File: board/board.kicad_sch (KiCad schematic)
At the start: 14 parts, among them J1 Conn_01x02_Socket, J2 Barrel_Jack_Switch, Q1 NPN, U1 LM350_TO3, U2 NE555P, U3 LM350_TO3

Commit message: add link on schematic
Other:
- note added: "https://www.electronicshub.org/555-timer-pwm/"
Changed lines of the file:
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@@
+    (effects (font (size 1.27 1.27)) (justify left bottom))
+  )
+  (text "https://www.electronicshub.org/555-timer-pwm/" (at 76.962 138.684 0)
     (effects (font (size 1.27 1.27)) (justify left bottom))
   )

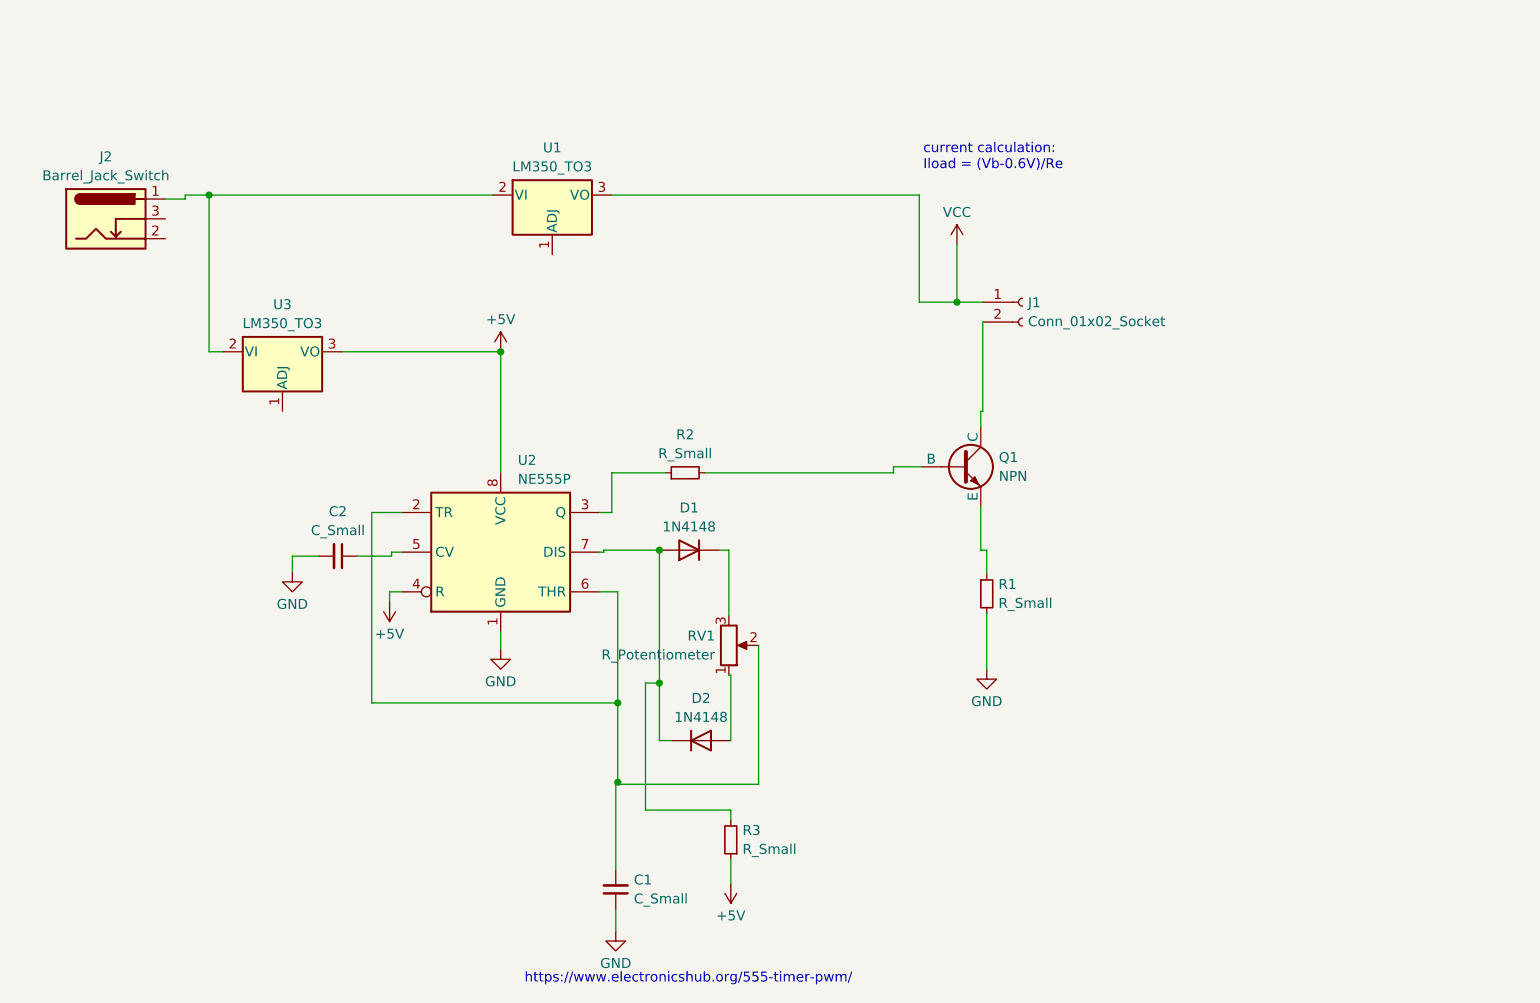
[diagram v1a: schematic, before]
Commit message: add first schematci version of LED driver
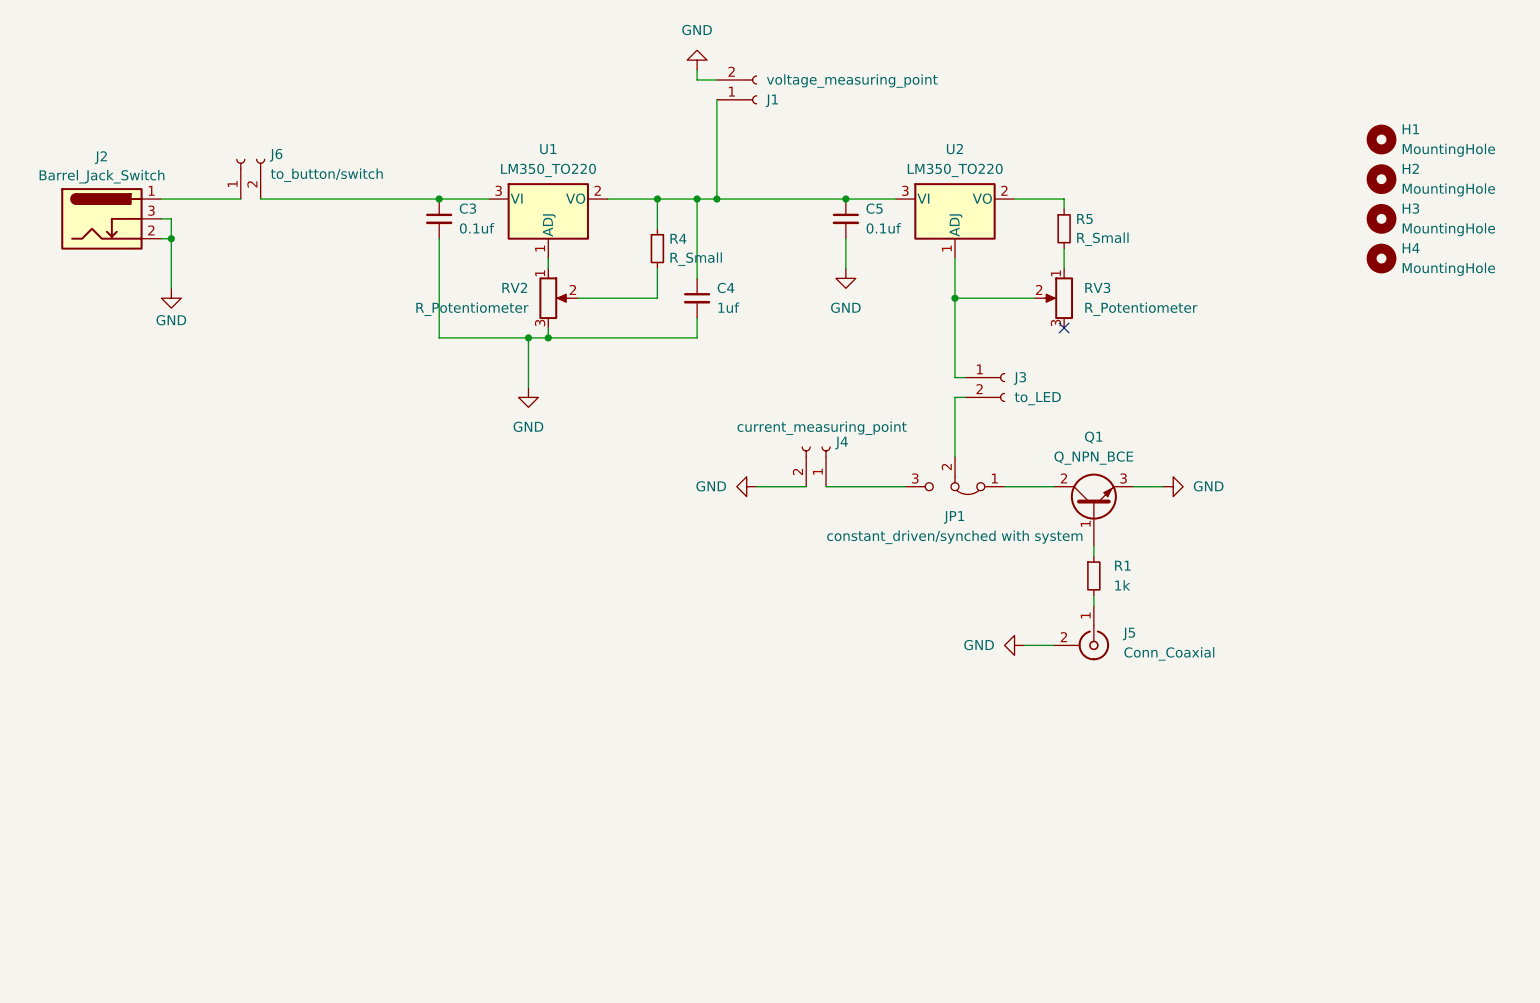
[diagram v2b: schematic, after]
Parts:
- removed C1, C2: C_Small, symbol Device:C_Small
- removed D1, D2: 1N4148, Diode_THT:D_DO-35_SOD27_P7.62mm_Horizontal, symbol Diode:1N4148
- removed Q1: NPN, symbol Simulation_SPICE:NPN
- removed R2, R3: R_Small, symbol Device:R_Small
- removed RV1: R_Potentiometer, symbol Device:R_Potentiometer
- removed U1, U3: LM350_TO3, Package_TO_SOT_THT:TO-3, symbol Regulator_Linear:LM350_TO3
- removed U2: NE555P, Package_DIP:DIP-8_W7.62mm, symbol Timer:NE555P
- added C3, C5: 0.1uf, Capacitor_THT:C_Disc_D9.0mm_W2.5mm_P5.00mm, symbol Device:C_Small
- added C4: 1uf, Capacitor_THT:CP_Radial_D10.0mm_P5.00mm, symbol Device:C_Small
- added H1, H2, H3, H4: MountingHole, MountingHole:MountingHole_3.2mm_M3, symbol Mechanical:MountingHole
- added J3: to_LED, Connector_JST:JST_XH_B2B-XH-A_1x02_P2.50mm_Vertical, symbol Connector:Conn_01x02_Socket
- added J4: current_measuring_point, Connector_JST:JST_XH_B2B-XH-A_1x02_P2.50mm_Vertical, symbol Connector:Conn_01x02_Socket
- added J5: Conn_Coaxial, Connector_JST:JST_XH_B2B-XH-A_1x02_P2.50mm_Vertical, symbol Connector:Conn_Coaxial
- added J6: to_button/switch, Connector_JST:JST_XH_B2B-XH-A_1x02_P2.50mm_Vertical, symbol Connector:Conn_01x02_Socket
- added JP1: constant_driven/synched with system, Connector_PinHeader_2.54mm:PinHeader_1x03_P2.54mm_Vertical, symbol Jumper:Jumper_3_Bridged12
- added Q1: Q_NPN_BCE, Package_TO_SOT_THT:TO-220-3_Vertical, symbol Device:Q_NPN_BCE
- added R4, R5: R_Small, Resistor_THT:R_Axial_DIN0411_L9.9mm_D3.6mm_P15.24mm_Horizontal, symbol Device:R_Small
- added RV2, RV3: R_Potentiometer, Connector_PinHeader_2.54mm:PinHeader_1x03_P2.54mm_Vertical, symbol Device:R_Potentiometer
- added U1, U2: LM350_TO220, Package_TO_SOT_THT:TO-220-3_Vertical, symbol Regulator_Linear:LM350_TO220
- J1: value Conn_01x02_Socket -> voltage_measuring_point; footprint (none) -> Connector_JST:JST_XH_B2B-XH-A_1x02_P2.50mm_Vertical
- J2: footprint (none) -> Connector_BarrelJack:BarrelJack_Horizontal
- R1: value R_Small -> 1k; footprint (none) -> Resistor_THT:R_Axial_DIN0411_L9.9mm_D3.6mm_P15.24mm_Horizontal
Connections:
- net GND: now also J1.2 (Pin_2), J2.2, J2.3, C3.2, C4.2, C5.2, J4.2 (Pin_2), J5.2 (Ext), Q1.3 (E), RV2.3; no longer R1.2
- net at R1.1: now also Q1.1 (B)
- net at J2.1: now also J6.1 (Pin_1)
- net VCC: no longer names the net of J1.1 (Pin_1)
- net VCC: now also C4.1, C5.1, R4.1, U1.2 (VO), U2.3 (VI)
- new net: J5.1 (In), R1.2
- new net: J3.1 (Pin_1), RV3.2, U2.1 (ADJ)
- new net: J3.2 (Pin_2), JP1.2 (C)
- new net: R5.1, U2.2 (VO)
- new net: R5.2, RV3.1
- new net: JP1.1 (A), Q1.2 (C)
- new net: J4.1 (Pin_1), JP1.3 (B)
- new net: RV2.1, U1.1 (ADJ)
- new net: C3.1, J6.2 (Pin_2), U1.3 (VI)
- new net: R4.2, RV2.2
- no-connect marks 0 -> 1
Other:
- note removed: "current calculation: Iload = (Vb-0.6V)/Re"
- note removed: "https://www.electronicshub.org/555-timer-pwm/"
- moved on the sheet: J2

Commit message: make first prototype and production files
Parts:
- removed J2: Barrel_Jack_Switch, Connector_BarrelJack:BarrelJack_Horizontal, symbol Connector:Barrel_Jack_Switch
- removed J6: to_button/switch, Connector_JST:JST_XH_B2B-XH-A_1x02_P2.50mm_Vertical, symbol Connector:Conn_01x02_Socket
- added D1: LED, LED_THT:LED_D5.0mm_Clear, symbol Device:LED
- added J2: Conn_01x03_Socket, Connector_JST:JST_XH_B3B-XH-A_1x03_P2.50mm_Vertical, symbol Connector:Conn_01x03_Socket
- added J7: Vin, Connector_JST:JST_XH_B2B-XH-A_1x02_P2.50mm_Vertical, symbol Connector:Conn_01x02_Socket
- added J8: Vin_relay, Connector_JST:JST_XH_B2B-XH-A_1x02_P2.50mm_Vertical, symbol Connector:Conn_01x02_Socket
- added R2: 1k, Resistor_THT:R_Axial_DIN0411_L9.9mm_D3.6mm_P15.24mm_Horizontal, symbol Device:R_Small
- added R3: 1M, Resistor_THT:R_Axial_DIN0411_L9.9mm_D3.6mm_P15.24mm_Horizontal, symbol Device:R_Small
- C4: symbol Device:C_Small -> Device:C_Polarized_Small
- R4: value R_Small -> 240
- R5: value R_Small -> 0.4ohm 2W
- RV2: value R_Potentiometer -> 5k
- RV3: value R_Potentiometer -> 10 ohm 2w
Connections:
- net GND: now also RV2.2, J2.3 (Pin_3), J7.2 (Pin_2), J8.2 (Pin_2), R2.1, R3.2; no longer RV2.3
- net at J3.1 (Pin_1), RV3.2, U2.1 (ADJ): now also R3.1
- net at RV2.1, U1.1 (ADJ): now also R4.2
- net at C3.1, U1.3 (VI): now also D1.2 (A), J2.2 (Pin_2)
- new net: D1.1 (K), R2.2
- new net +12V: J2.1 (Pin_1), J7.1 (Pin_1), J8.1 (Pin_1)
- no-connect marks 1 -> 2
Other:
- moved on the sheet: RV2

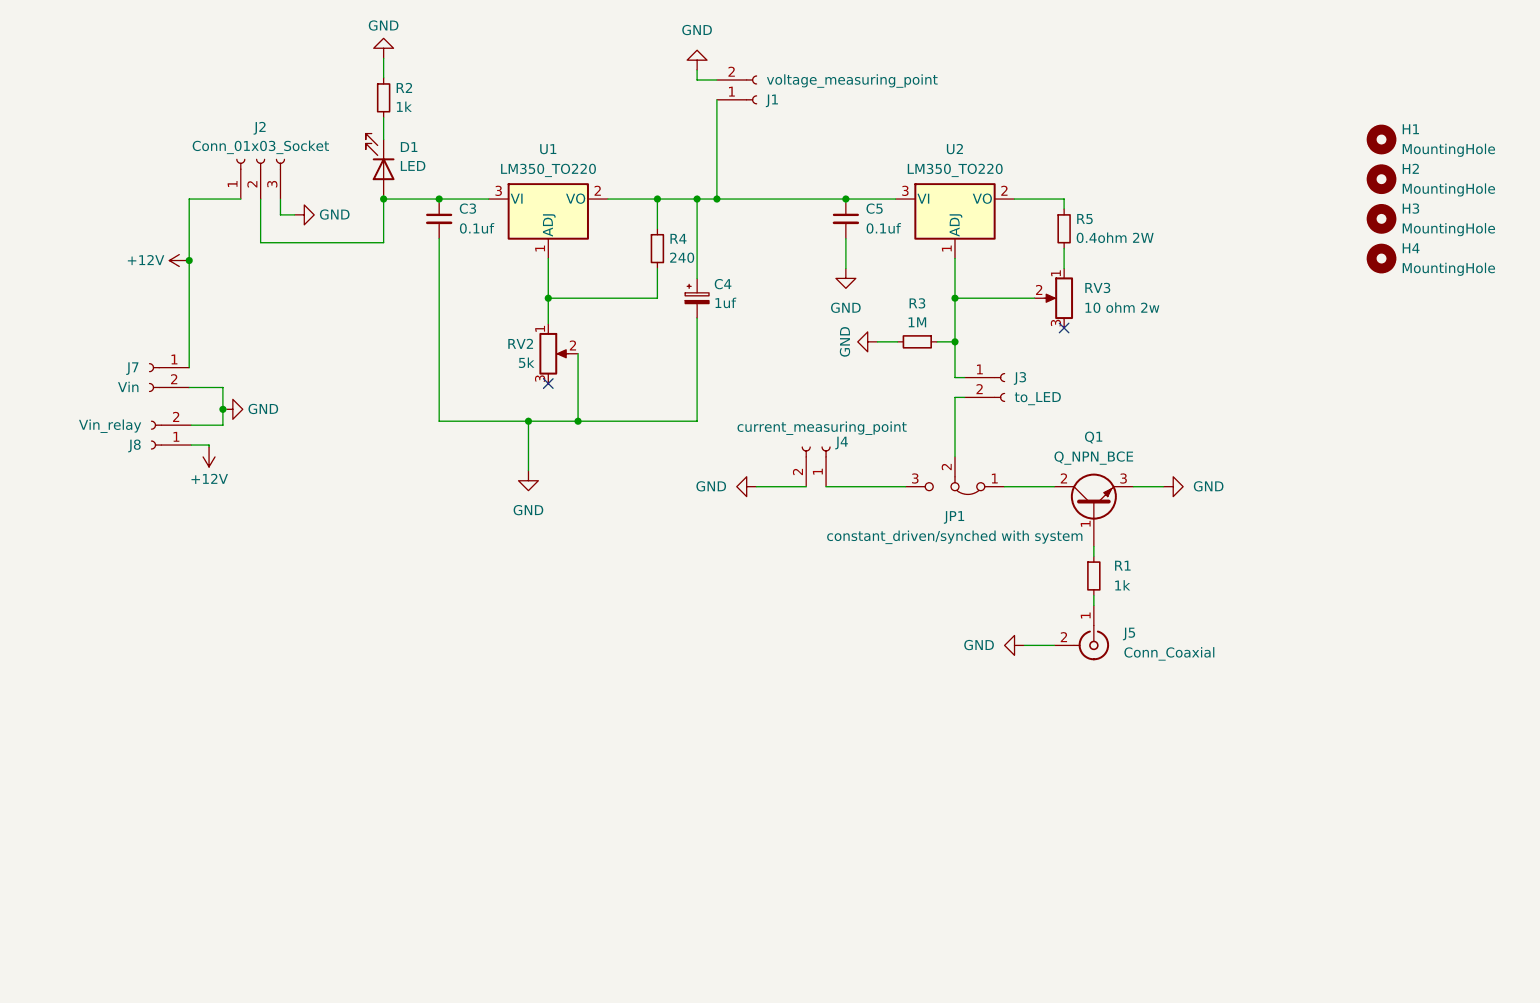
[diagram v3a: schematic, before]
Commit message: new design for led Driver
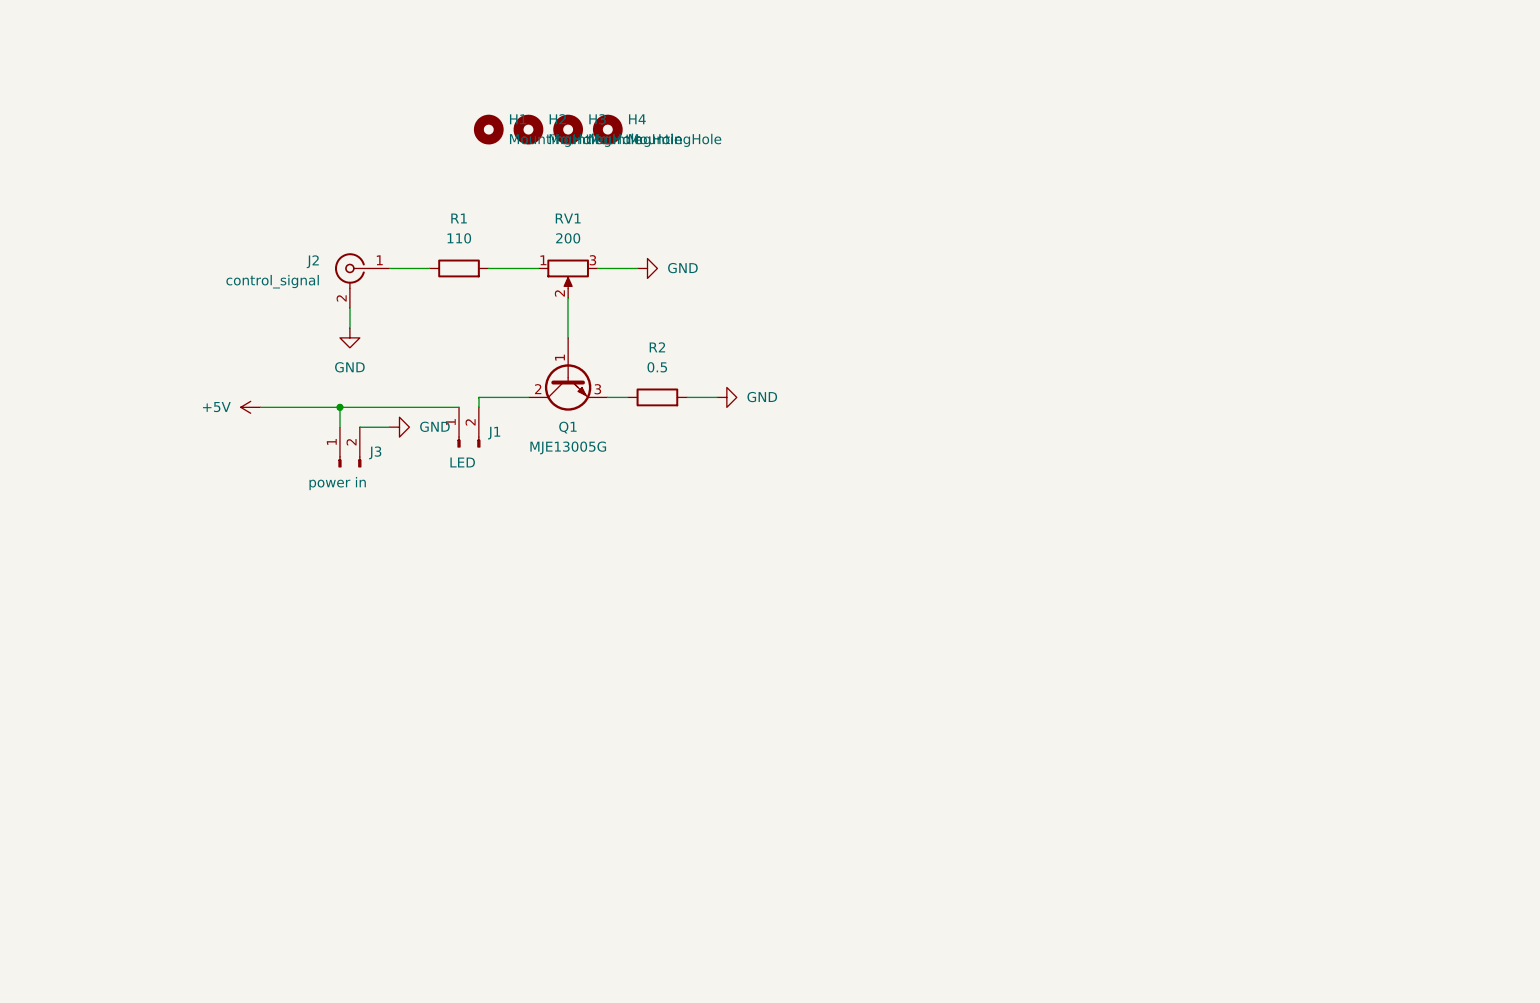
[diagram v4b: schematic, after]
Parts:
- removed C3, C5: 0.1uf, Capacitor_THT:C_Disc_D9.0mm_W2.5mm_P5.00mm, symbol Device:C_Small
- removed C4: 1uf, Capacitor_THT:CP_Radial_D10.0mm_P5.00mm, symbol Device:C_Polarized_Small
- removed D1: LED, LED_THT:LED_D5.0mm_Clear, symbol Device:LED
- removed J1: voltage_measuring_point, Connector_JST:JST_XH_B2B-XH-A_1x02_P2.50mm_Vertical, symbol Connector:Conn_01x02_Socket
- removed J2: Conn_01x03_Socket, Connector_JST:JST_XH_B3B-XH-A_1x03_P2.50mm_Vertical, symbol Connector:Conn_01x03_Socket
- removed J3: to_LED, Connector_JST:JST_XH_B2B-XH-A_1x02_P2.50mm_Vertical, symbol Connector:Conn_01x02_Socket
- removed J4: current_measuring_point, Connector_JST:JST_XH_B2B-XH-A_1x02_P2.50mm_Vertical, symbol Connector:Conn_01x02_Socket
- removed J5: Conn_Coaxial, Connector_JST:JST_XH_B2B-XH-A_1x02_P2.50mm_Vertical, symbol Connector:Conn_Coaxial
- removed J7: Vin, Connector_JST:JST_XH_B2B-XH-A_1x02_P2.50mm_Vertical, symbol Connector:Conn_01x02_Socket
- removed J8: Vin_relay, Connector_JST:JST_XH_B2B-XH-A_1x02_P2.50mm_Vertical, symbol Connector:Conn_01x02_Socket
- removed JP1: constant_driven/synched with system, Connector_PinHeader_2.54mm:PinHeader_1x03_P2.54mm_Vertical, symbol Jumper:Jumper_3_Bridged12
- removed Q1: Q_NPN_BCE, Package_TO_SOT_THT:TO-220-3_Vertical, symbol Device:Q_NPN_BCE
- removed R1, R2: 1k, Resistor_THT:R_Axial_DIN0411_L9.9mm_D3.6mm_P15.24mm_Horizontal, symbol Device:R_Small
- removed R3: 1M, Resistor_THT:R_Axial_DIN0411_L9.9mm_D3.6mm_P15.24mm_Horizontal, symbol Device:R_Small
- removed R4: 240, Resistor_THT:R_Axial_DIN0411_L9.9mm_D3.6mm_P15.24mm_Horizontal, symbol Device:R_Small
- removed R5: 0.4ohm 2W, Resistor_THT:R_Axial_DIN0411_L9.9mm_D3.6mm_P15.24mm_Horizontal, symbol Device:R_Small
- removed RV2: 5k, Connector_PinHeader_2.54mm:PinHeader_1x03_P2.54mm_Vertical, symbol Device:R_Potentiometer
- removed RV3: 10 ohm 2w, Connector_PinHeader_2.54mm:PinHeader_1x03_P2.54mm_Vertical, symbol Device:R_Potentiometer
- removed U1, U2: LM350_TO220, Package_TO_SOT_THT:TO-220-3_Vertical, symbol Regulator_Linear:LM350_TO220
- added J1: LED, Connector_JST:JST_XH_B2B-XH-A_1x02_P2.50mm_Vertical, symbol Connector:Conn_01x02_Pin
- added J2: control_signal, Connector_JST:JST_XH_B2B-XH-A_1x02_P2.50mm_Vertical, symbol Connector:Conn_Coaxial
- added J3: power in, Connector_JST:JST_XH_B2B-XH-A_1x02_P2.50mm_Vertical, symbol Connector:Conn_01x02_Pin
- added Q1: MJE13005G, Package_TO_SOT_THT:TO-220-3_Vertical, symbol Transistor_BJT:MJE13005G
- added R1: 110, Resistor_THT:R_Axial_DIN0411_L9.9mm_D3.6mm_P15.24mm_Horizontal, symbol Device:R
- added R2: 0.5, Package_TO_SOT_THT:TO-220-2_Vertical, symbol Device:R
- added RV1: 200, Connector_JST:JST_XH_B3B-XH-A_1x03_P2.50mm_Vertical, symbol Device:R_Potentiometer
- H1, H2, H3, H4: now left out of the parts list
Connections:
- net GND: now also J2.2 (Ext), J3.2 (Pin_2), R2.2, RV1.3
- new net: R1.2, RV1.1
- new net: Q1.1 (B), RV1.2
- new net: Q1.3 (E), R2.1
- new net: J2.1 (In), R1.1
- new net: J1.2 (Pin_2), Q1.2 (C)
- new net +5V: J1.1 (Pin_1), J3.1 (Pin_1)
- no-connect marks 2 -> 0

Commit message: save small design changes just descriobed
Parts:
- added R3: 0.5, Resistor_THT:R_Axial_DIN0414_L11.9mm_D4.5mm_P15.24mm_Horizontal, symbol Device:R
- added R4: 0.5, Resistor_THT:R_Axial_Power_L38.0mm_W9.0mm_P45.72mm, symbol Device:R
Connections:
- net GND: now also R3.2, R4.2
- net at Q1.3 (E), R2.1: now also R3.1, R4.1
